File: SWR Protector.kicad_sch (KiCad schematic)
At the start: 29 parts, among them J1 Barrel_Jack, J2 Barrel_Jack, J3 transceiver, J4 antenna, K2 ATX209, Q1 2N3904, T1 1:12, T2 1:12, U1 LM78L05_TO92, U2 LM358

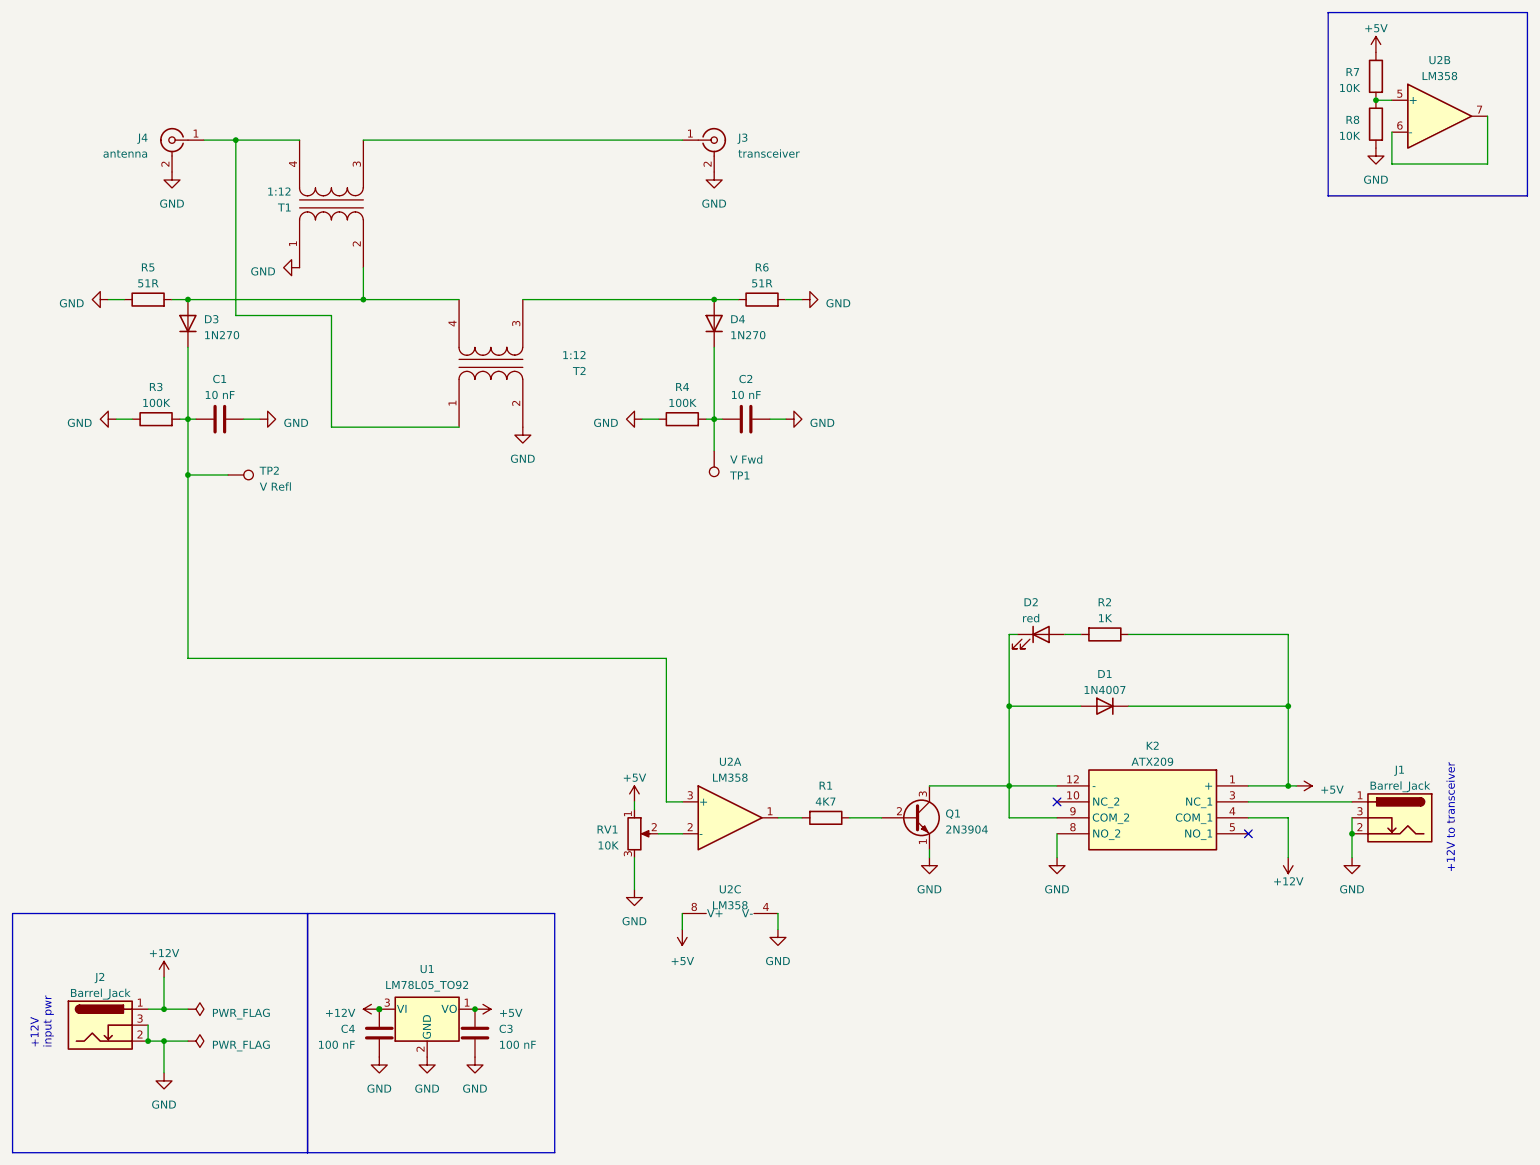
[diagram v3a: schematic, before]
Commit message: added header for pwr/gnd and both fwd and rev for microcontroler
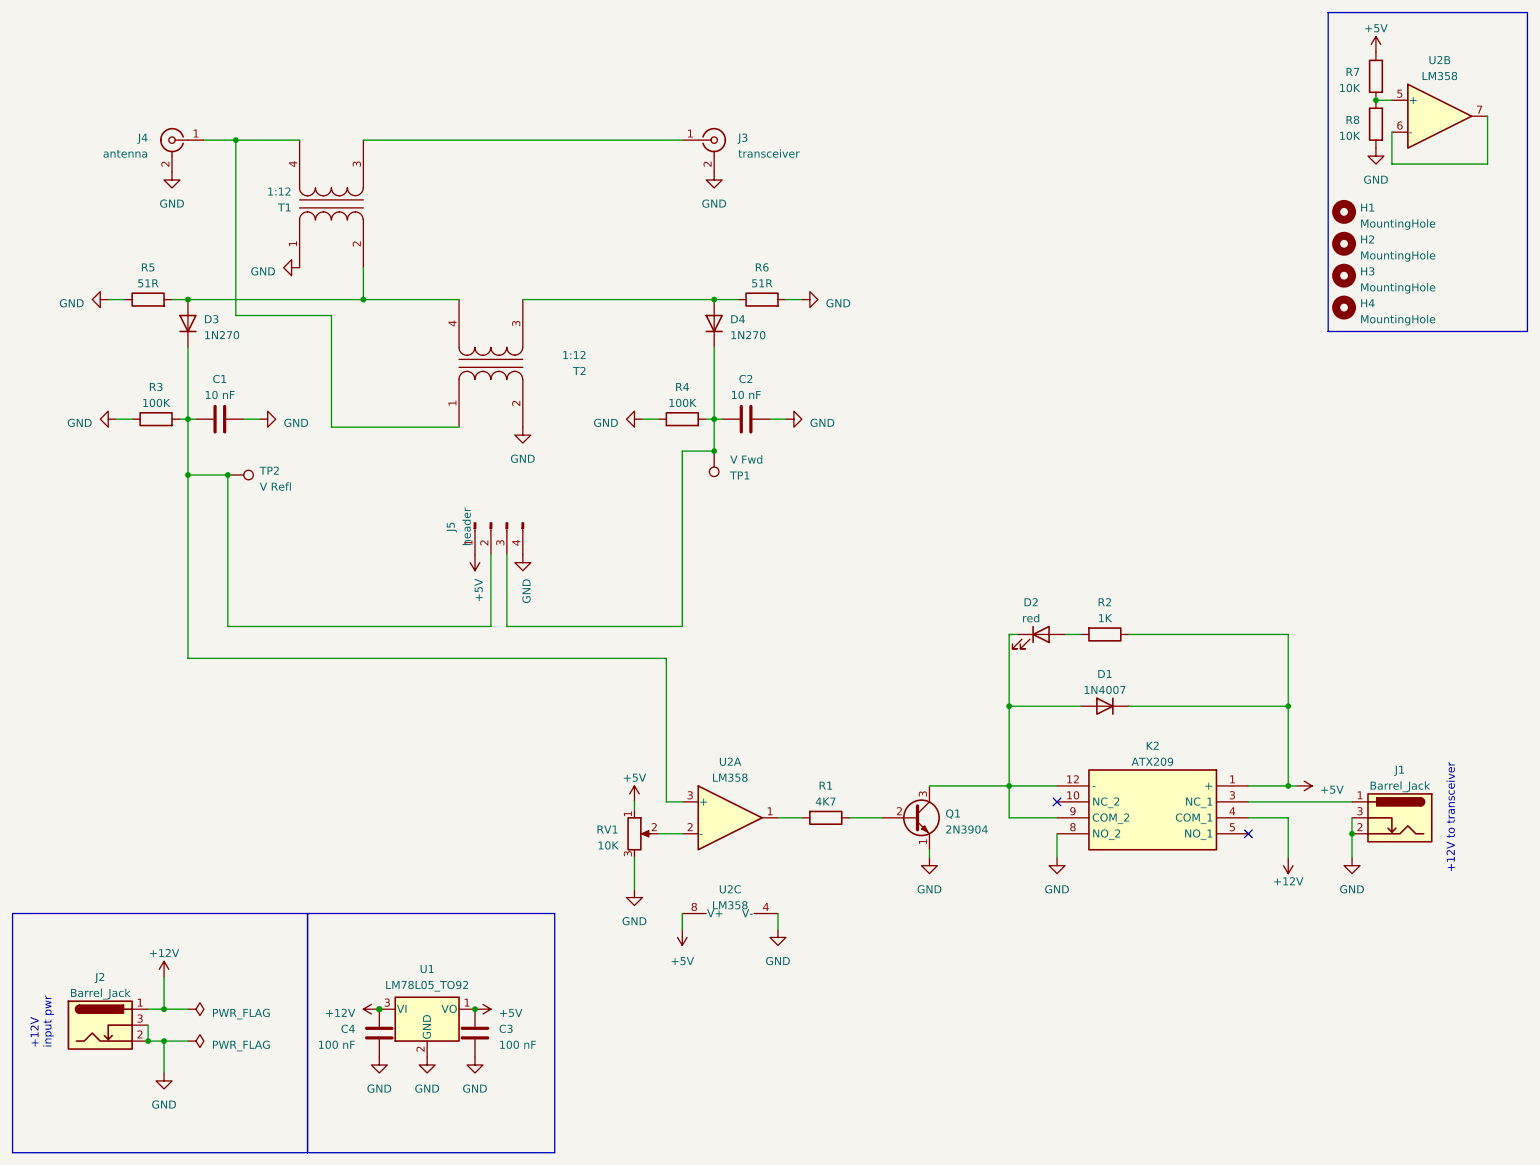
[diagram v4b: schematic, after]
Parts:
- added H1, H2, H3, H4: MountingHole, MountingHole:MountingHole_4.3mm_M4, symbol Mechanical:MountingHole
- added J5: header, Connector_PinHeader_2.54mm:PinHeader_1x04_P2.54mm_Vertical, symbol Connector:Conn_01x04_Pin
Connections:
- net +5V: now also J5.1 (Pin_1)
- net GND: now also J5.4 (Pin_4)
- net at C2.1, D4.1 (K), R4.2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: now also J5.3 (Pin_3)
- net at C1.1, D3.1 (K), R3.2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: now also J5.2 (Pin_2)
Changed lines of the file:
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@@
   (junction (at 44.45 179.07) (diameter 0) (color 0 0 0 0)
   )
+  (junction (at 57.15 88.9) (diameter 0) (color 0 0 0 0)
+  )
   (junction (at 181.61 138.43) (diameter 0) (color 0 0 0 0)
   )
@@
   )
   (junction (at 46.99 179.07) (diameter 0) (color 0 0 0 0)
+  )
+  (junction (at 134.62 85.09) (diameter 0) (color 0 0 0 0)
   )
   (junction (at 226.06 125.73) (diameter 0) (color 0 0 0 0)
@@
     (stroke (width 0) (type default))
   )
+  (wire (pts (xy 134.62 85.09) (xy 129.54 85.09))
+    (stroke (width 0) (type default))
+  )
+  (wire (pts (xy 129.54 113.03) (xy 101.6 113.03))
+    (stroke (width 0) (type default))
+  )
   (wire (pts (xy 39.37 80.01) (xy 41.91 80.01))
     (stroke (width 0) (type default))
@@
     (stroke (width 0) (type default))
   )
+  (wire (pts (xy 57.15 88.9) (xy 57.15 113.03))
+    (stroke (width 0) (type default))
+  )
   (wire (pts (xy 190.5 114.3) (xy 193.04 114.3))
     (stroke (width 0) (type default))
@@
     (stroke (width 0) (type default))
   )
+  (wire (pts (xy 101.6 101.6) (xy 101.6 113.03))
+    (stroke (width 0) (type default))
+  )
   (wire (pts (xy 168.91 138.43) (xy 181.61 138.43))
     (stroke (width 0) (type default))
@@
     (stroke (width 0) (type default))
   )
+  (wire (pts (xy 57.15 113.03) (xy 99.06 113.03))
+    (stroke (width 0) (type default))
+  )
   (wire (pts (xy 226.06 138.43) (xy 227.33 138.43))
     (stroke (width 0) (type default))
@@
     (stroke (width 0) (type default))
   )
+  (wire (pts (xy 99.06 113.03) (xy 99.06 101.6))
+    (stroke (width 0) (type default))
+  )
   (wire (pts (xy 226.06 114.3) (xy 200.66 114.3))
     (stroke (width 0) (type default))
@@
     (stroke (width 0) (type default))
   )
+  (wire (pts (xy 129.54 85.09) (xy 129.54 113.03))
+    (stroke (width 0) (type default))
+  )
   (wire (pts (xy 123.19 80.01) (xy 125.73 80.01))
     (stroke (width 0) (type default))
@@
     (fill (type none))
   )
-  (rectangle (start 232.41 15.24) (end 264.16 44.45)
+  (rectangle (start 232.41 15.24) (end 264.16 66.04)
     (stroke (width 0) (type default))
     (fill (type none))
@@
     )
   )
+  (symbol (lib_id "Mechanical:MountingHole") (at 234.95 57.15 0) (unit 1)
+    (in_bom yes) (on_board yes) (dnp no) (fields_autoplaced)
+    (property "Reference" "H3" (at 237.49 56.515 0)
+      (effects (font (size 1.27 1.27)) (justify left))
+    )
+    (property "Value" "MountingHole" (at 237.49 59.055 0)
+      (effects (font (size 1.27 1.27)) (justify left))
+    )
+    (property "Footprint" "MountingHole:MountingHole_4.3mm_M4" (at 234.95 57.15 0)
+      (effects (font (size 1.27 1.27)) hide)
+    )
+    (property "Datasheet" "~" (at 234.95 57.15 0)
+      (effects (font (size 1.27 1.27)) hide)
+    )
+    (instances
+      (project "SWR Protector"
+        (path "/46027dd5-036f-43c6-98e1-c4cfe473ecd7"
+          (reference "H3") (unit 1)
+        )
+      )
+    )
+  )
   (symbol (lib_id "power:GND") (at 146.05 80.01 90) (mirror x) (unit 1)
     (in_bom yes) (on_board yes) (dnp no)
@@
     )
   )
+  (symbol (lib_id "Mechanical:MountingHole") (at 234.95 46.99 0) (unit 1)
+    (in_bom yes) (on_board yes) (dnp no) (fields_autoplaced)
+    (property "Reference" "H1" (at 237.49 46.355 0)
+      (effects (font (size 1.27 1.27)) (justify left))
+    )
+    (property "Value" "MountingHole" (at 237.49 48.895 0)
+      (effects (font (size 1.27 1.27)) (justify left))
+    )
+    (property "Footprint" "MountingHole:MountingHole_4.3mm_M4" (at 234.95 46.99 0)
+      (effects (font (size 1.27 1.27)) hide)
+    )
+    (property "Datasheet" "~" (at 234.95 46.99 0)
+      (effects (font (size 1.27 1.27)) hide)
+    )
+    (instances
+      (project "SWR Protector"
+        (path "/46027dd5-036f-43c6-98e1-c4cfe473ecd7"
+          (reference "H1") (unit 1)
+        )
+      )
+    )
+  )
   (symbol (lib_id "power:+5V") (at 96.52 173.99 270) (unit 1)
     (in_bom yes) (on_board yes) (dnp no) (fields_autoplaced)
@@
         (path "/46027dd5-036f-43c6-98e1-c4cfe473ecd7"
           (reference "C1") (unit 1)
+        )
+      )
+    )
+  )
+  (symbol (lib_id "Connector:Conn_01x04_Pin") (at 99.06 96.52 90) (mirror x) (unit 1)
+    (in_bom yes) (on_board yes) (dnp no) (fields_autoplaced)
+    (property "Reference" "J5" (at 92.71 97.155 0)
+      (effects (font (size 1.27 1.27)))
+    )
+    (property "Value" "header" (at 95.25 97.155 0)
+      (effects (font (size 1.27 1.27)))
+    )
+    (property "Footprint" "Connector_PinHeader_2.54mm:PinHeader_1x04_P2.54mm_Vertical" (at 99.06 96.52 0)
+      (effects (font (size 1.27 1.27)) hide)
+    )
+    (property "Datasheet" "~" (at 99.06 96.52 0)
+      (effects (font (size 1.27 1.27)) hide)
+    )
+    (pin "1")
+    (pin "2")
+    (pin "3")
+    (pin "4")
+    (instances
+      (project "SWR Protector"
+        (path "/46027dd5-036f-43c6-98e1-c4cfe473ecd7"
+          (reference "J5") (unit 1)
         )
       )
@@
         (path "/46027dd5-036f-43c6-98e1-c4cfe473ecd7"
           (reference "D3") (unit 1)
+        )
+      )
+    )
+  )
+  (symbol (lib_id "Mechanical:MountingHole") (at 234.95 62.23 0) (unit 1)
+    (in_bom yes) (on_board yes) (dnp no) (fields_autoplaced)
+    (property "Reference" "H4" (at 237.49 61.595 0)
+      (effects (font (size 1.27 1.27)) (justify left))
+    )
+    (property "Value" "MountingHole" (at 237.49 64.135 0)
+      (effects (font (size 1.27 1.27)) (justify left))
+    )
+    (property "Footprint" "MountingHole:MountingHole_4.3mm_M4" (at 234.95 62.23 0)
+      (effects (font (size 1.27 1.27)) hide)
+    )
+    (property "Datasheet" "~" (at 234.95 62.23 0)
+      (effects (font (size 1.27 1.27)) hide)
+    )
+    (instances
+      (project "SWR Protector"
+        (path "/46027dd5-036f-43c6-98e1-c4cfe473ecd7"
+          (reference "H4") (unit 1)
         )
       )
@@
     )
   )
+  (symbol (lib_id "Mechanical:MountingHole") (at 234.95 52.07 0) (unit 1)
+    (in_bom yes) (on_board yes) (dnp no) (fields_autoplaced)
+    (property "Reference" "H2" (at 237.49 51.435 0)
+      (effects (font (size 1.27 1.27)) (justify left))
+    )
+    (property "Value" "MountingHole" (at 237.49 53.975 0)
+      (effects (font (size 1.27 1.27)) (justify left))
+    )
+    (property "Footprint" "MountingHole:MountingHole_4.3mm_M4" (at 234.95 52.07 0)
+      (effects (font (size 1.27 1.27)) hide)
+    )
+    (property "Datasheet" "~" (at 234.95 52.07 0)
+      (effects (font (size 1.27 1.27)) hide)
+    )
+    (instances
+      (project "SWR Protector"
+        (path "/46027dd5-036f-43c6-98e1-c4cfe473ecd7"
+          (reference "H2") (unit 1)
+        )
+      )
+    )
+  )
   (symbol (lib_id "Device:C") (at 81.28 177.8 0) (mirror y) (unit 1)
     (in_bom yes) (on_board yes) (dnp no)
@@
         (path "/46027dd5-036f-43c6-98e1-c4cfe473ecd7"
           (reference "R3") (unit 1)
+        )
+      )
+    )
+  )
+  (symbol (lib_id "power:GND") (at 104.14 101.6 0) (mirror y) (unit 1)
+    (in_bom yes) (on_board yes) (dnp no) (fields_autoplaced)
+    (property "Reference" "#PWR030" (at 104.14 107.95 0)
+      (effects (font (size 1.27 1.27)) hide)
+    )
+    (property "Value" "GND" (at 104.775 105.41 90)
+      (effects (font (size 1.27 1.27)) (justify right))
+    )
+    (property "Footprint" "" (at 104.14 101.6 0)
+      (effects (font (size 1.27 1.27)) hide)
+    )
+    (property "Datasheet" "" (at 104.14 101.6 0)
+      (effects (font (size 1.27 1.27)) hide)
+    )
+    (pin "1")
+    (instances
+      (project "SWR Protector"
+        (path "/46027dd5-036f-43c6-98e1-c4cfe473ecd7"
+          (reference "#PWR030") (unit 1)
         )
       )
@@
         )
       )
+    )
+  )
+  (symbol (lib_id "power:+5V") (at 96.52 101.6 0) (mirror x) (unit 1)
+    (in_bom yes) (on_board yes) (dnp no) (fields_autoplaced)
+    (property "Reference" "#PWR029" (at 96.52 97.79 0)
+      (effects (font (size 1.27 1.27)) hide)
+    )
+    (property "Value" "+5V" (at 97.155 105.41 90)
+      (effects (font (size 1.27 1.27)) (justify left))
+    )
+    (property "Footprint" "" (at 96.52 101.6 0)
+      (effects (font (size 1.27 1.27)) hide)
+    )
+    (property "Datasheet" "" (at 96.52 101.6 0)
+      (effects (font (size 1.27 1.27)) hide)
+    )
+    (pin "1")
+    (instances
+      (project "SWR Protector"
+        (path "/46027dd5-036f-43c6-98e1-c4cfe473ecd7"
+          (reference "#PWR029") (unit 1)
+        )
+      )

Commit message: v0.8 massive changes.  Start with 1593L board, imported schematic, updated symbol libs and footprint libs.  Working on layout now. Dropped testpoints as we have them on the header now.  Diodes and resistors all went vertical to save space.  LED is horizontal so it pokes out the faceplate near switched power.
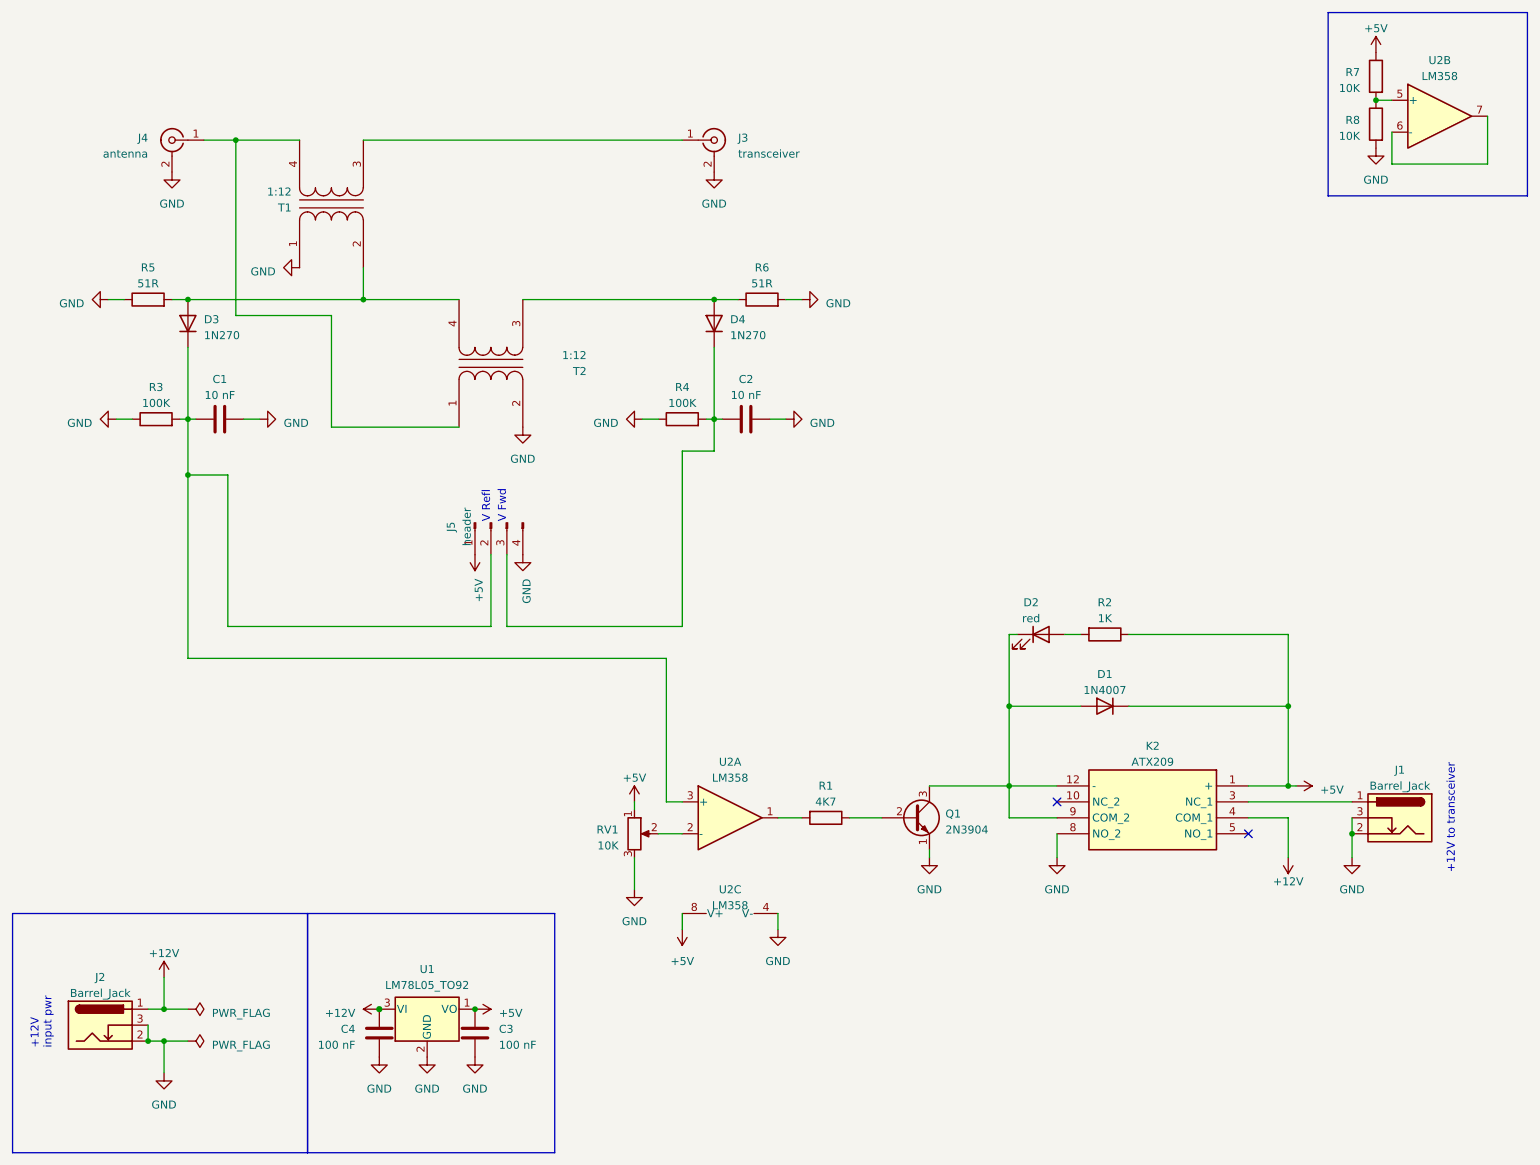
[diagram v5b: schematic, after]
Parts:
- removed H1, H2, H3, H4: MountingHole, MountingHole:MountingHole_4.3mm_M4, symbol Mechanical:MountingHole
- removed TP1: V Fwd, TestPoint:TestPoint_THTPad_4.0x4.0mm_Drill2.0mm, symbol Connector:TestPoint
- removed TP2: V Refl, TestPoint:TestPoint_THTPad_4.0x4.0mm_Drill2.0mm, symbol Connector:TestPoint
- D1, D3, D4: footprint Diode_THT:D_DO-41_SOD81_P10.16mm_Horizontal -> Diode_THT:D_DO-15_P3.81mm_Vertical_KathodeUp
- D2: footprint LED_THT:LED_D5.0mm -> LED_THT:LED_D5.0mm_Horizontal_O1.27mm_Z9.0mm
- K2: footprint KiCad:ATX209 -> ATX209:ATX209
- R1, R2, R3, R4, R5, R6, R7, R8: footprint Resistor_THT:R_Axial_DIN0207_L6.3mm_D2.5mm_P7.62mm_Horizontal -> Resistor_THT:R_Axial_DIN0207_L6.3mm_D2.5mm_P2.54mm_Vertical
- U2: footprint KiCAD:LM358 -> LM358:ON_Semiconductor-626-05-04_2015-P-MFG
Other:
- note added: "V Fwd"
- note added: "V Refl"
